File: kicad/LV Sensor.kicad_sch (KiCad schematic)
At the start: 4 parts, among them U1 MCP2518FD-xQBB, U2 74LVC1G3157, U3 MSPM0C1104SDSGR, U4 ADS8689RUM

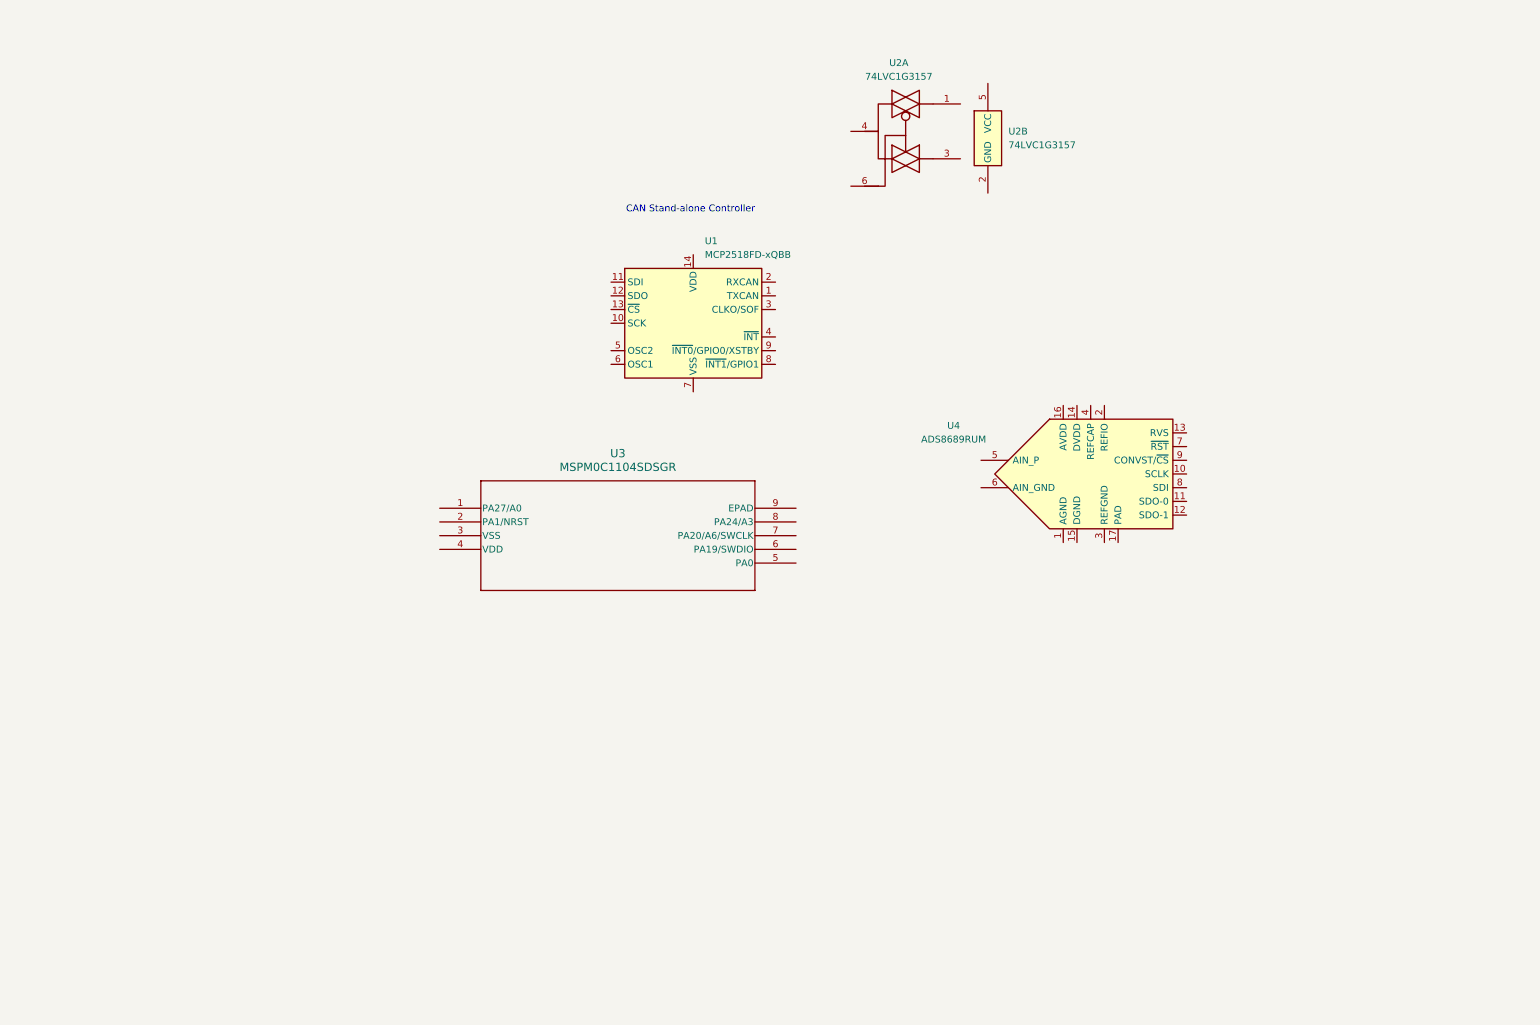
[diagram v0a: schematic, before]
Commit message: 08-25-25 Updated Board
Everything got deleted because a new copy was saved elsewhere.
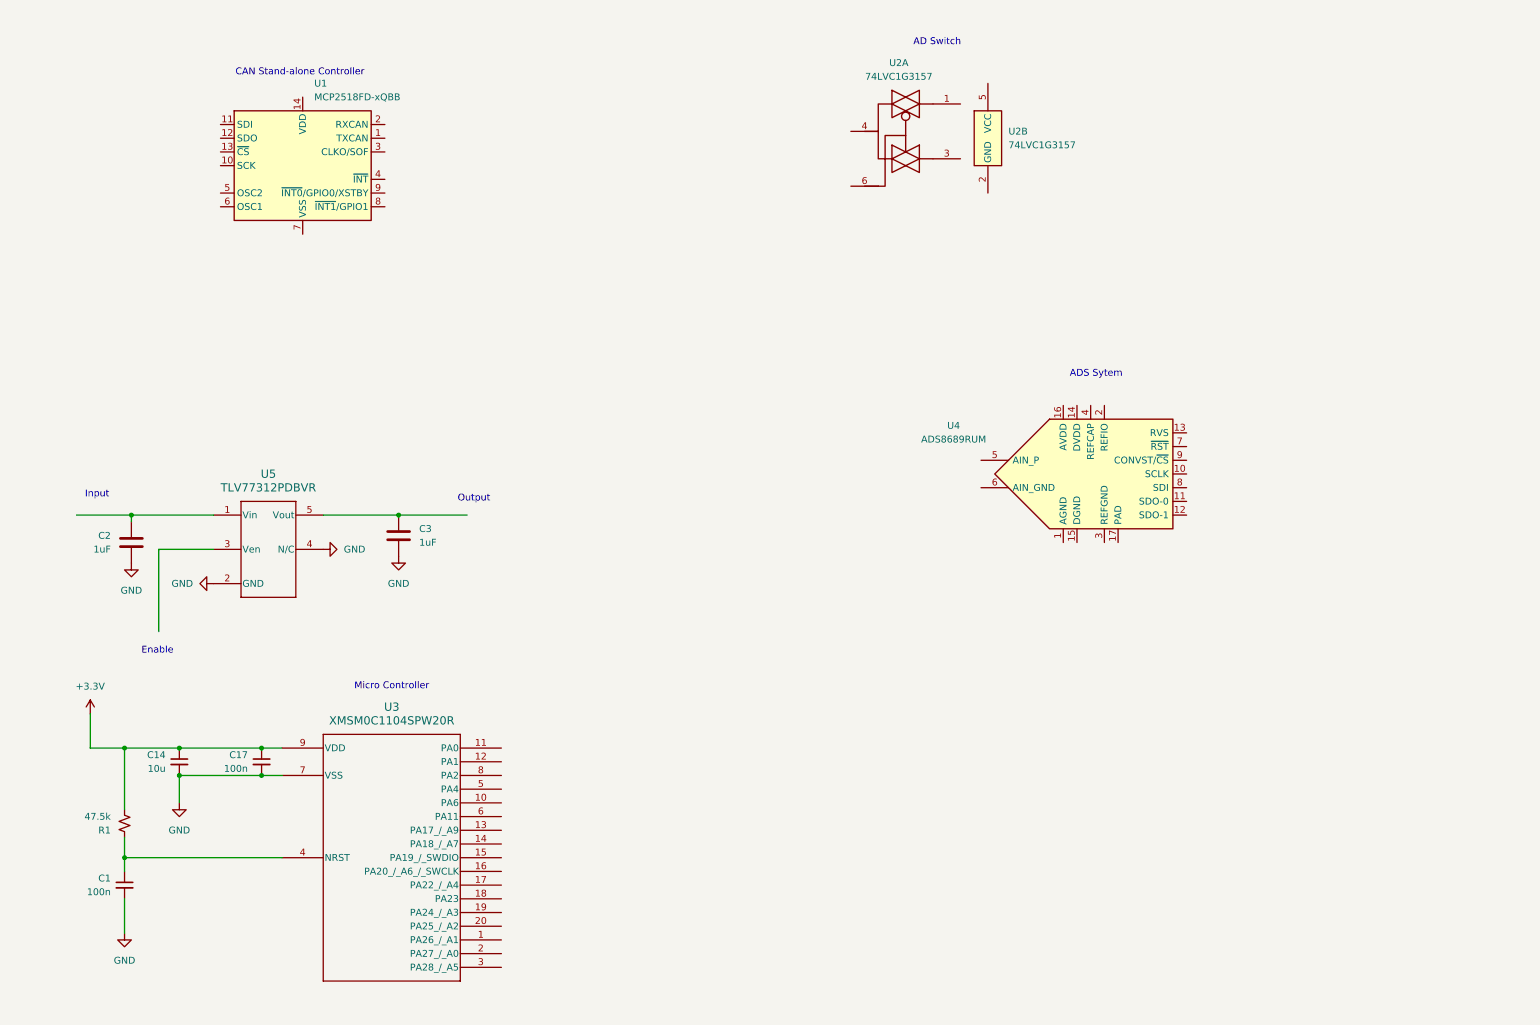
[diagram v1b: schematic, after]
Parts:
- removed U3: MSPM0C1104SDSGR, DSG0008A_TEX, symbol MSPM0C1104SDSGR:MSPM0C1104SDSGR
- added C1, C17: 100n, Capacitor_SMD:C_1206_3216Metric_Pad1.33x1.80mm_HandSolder, symbol Device:C_Small
- added C14: 10u, Capacitor_SMD:C_1206_3216Metric_Pad1.33x1.80mm_HandSolder, symbol Device:C_Small
- added C2, C3: 1uF, symbol Device:C
- added R1: 47.5k, Resistor_SMD:R_1206_3216Metric_Pad1.30x1.75mm_HandSolder, symbol Device:R_Small_US
- added U3: XMSM0C1104SPW20R, TSSOP20_PW_TEX, symbol MSPM0C1104-TSSOP:XMSM0C1104SPW20R
- added U5: TLV77312PDBVR, DBV0005A-IPC_A, symbol TLV77333PDBVR:TLV77312PDBVR
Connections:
- new net: C2.1, U5.1 (Vin)
- new net: C3.1, U5.5 (Vout)
- new net: C1.1, R1.1, U3.4 (NRST)
- new net +3.3V: C14.1, C17.1, R1.2, U3.9 (VDD)
- new net GND: C1.2, C14.2, C17.2, C2.2, C3.2, U3.7 (VSS), U5.2 (GND), U5.4 (N/C)
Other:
- note added: "AD Switch"
- note added: "ADS Sytem"
- note added: "Enable"
- note added: "Input"
- note added: "Micro Controller"
- note added: "Output"
- moved on the sheet: U1

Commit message: 06-26-25 Added OP Amplifier to schematic
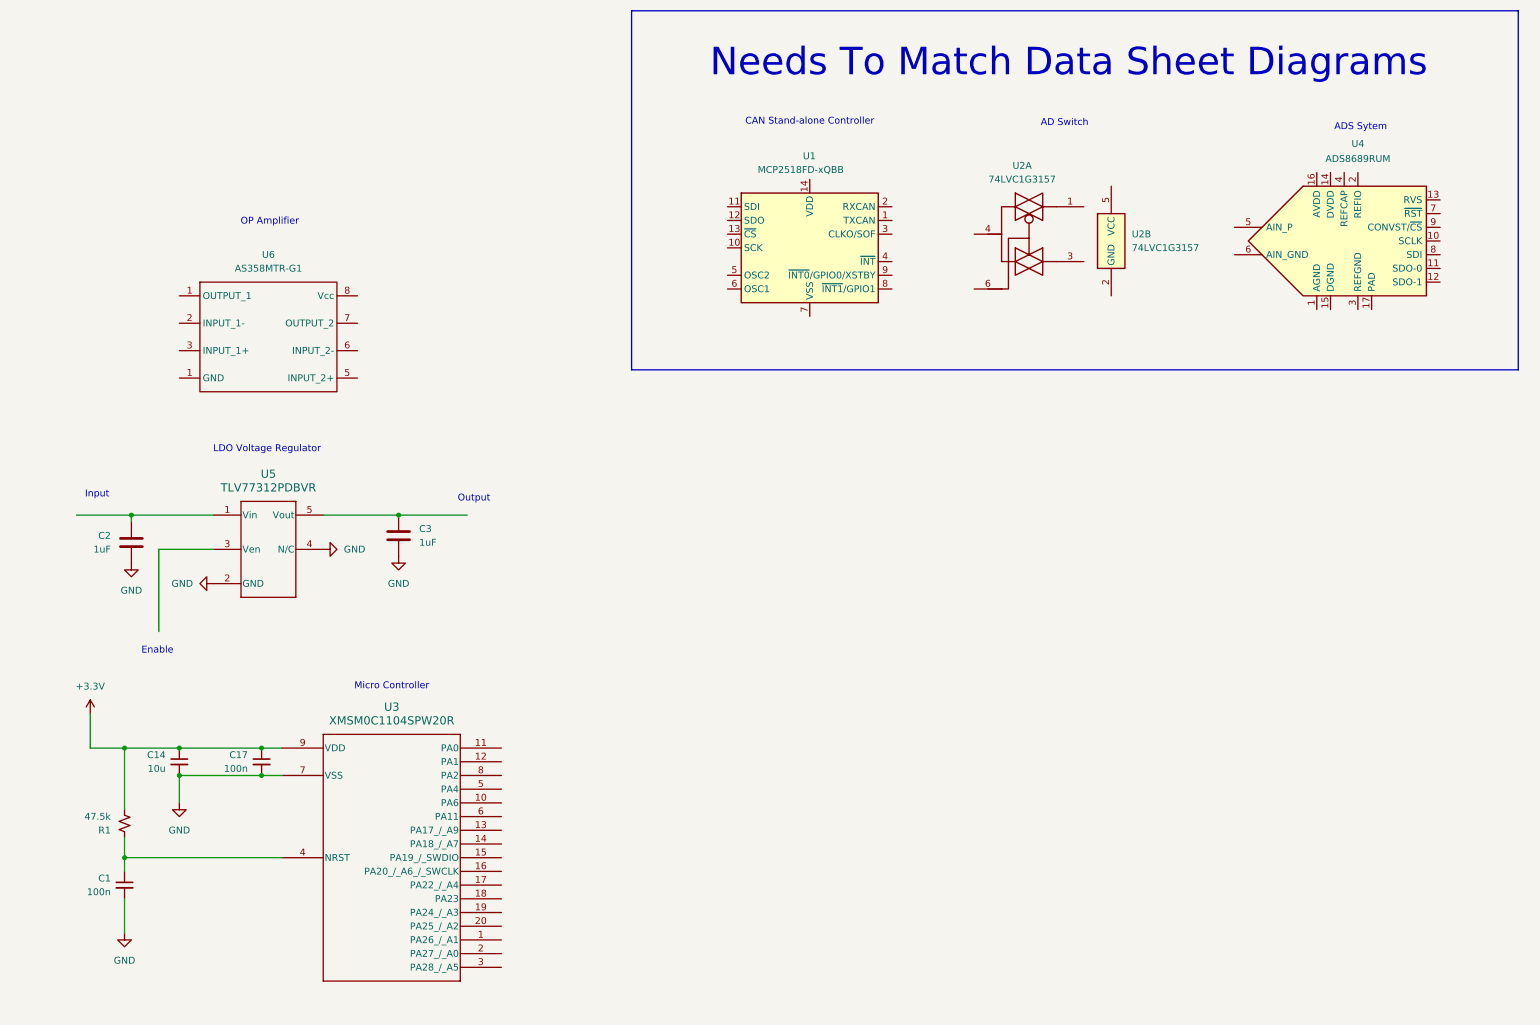
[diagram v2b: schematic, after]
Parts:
- added U6: AS358MTR-G1, symbol LV-Sensor-Lib:AS358MTR-G1
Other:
- note added: "LDO Voltage Regulator"
- note added: "Needs To Match Data Sheet Diagrams"
- note added: "OP Amplifier"
- company: (none) -> UTA FSAE
- title: (none) -> Low Voltage Sensor
- moved on the sheet: U1, U2A, U2B, U4
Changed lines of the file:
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@@
 	(generator_version "9.0")
 	(paper "A4")
+	(title_block
+		(title "Low Voltage Sensor")
+		(date "08-22-25")
+		(rev "0.1")
+		(company "UTA FSAE")
+	)
+	(rectangle
+		(start 120.65 11.938)
+		(end 284.988 78.486)
+		(stroke
+			(width 0)
+			(type default)
+		)
+		(fill
+			(type none)
+		)
+	)
 	(text "AD Switch"
 		(exclude_from_sim no)
-		(at 177.292 17.78 0)
+		(at 200.914 32.766 0)
+		(effects
+			(font
+				(size 1.27 1.27)
+			)
+		)
+	)
+	(text "LDO Voltage Regulator"
+		(exclude_from_sim no)
+		(at 53.086 93.218 0)
 		(effects
 			(font
@@
 	(text "CAN Stand-alone Controller"
 		(exclude_from_sim no)
-		(at 59.182 23.368 0)
+		(at 153.67 32.512 0)
 		(effects
 			(font
@@
 	(text "ADS Sytem"
 		(exclude_from_sim no)
-		(at 206.756 79.248 0)
+		(at 255.778 33.528 0)
 		(effects
 			(font
@@
 		(exclude_from_sim no)
 		(at 91.44 102.362 0)
+		(effects
+			(font
+				(size 1.27 1.27)
+			)
+		)
+	)
+	(text "Needs To Match Data Sheet Diagrams"
+		(exclude_from_sim no)
+		(at 201.676 21.59 0)
+		(effects
+			(font
+				(size 5.08 5.08)
+			)
+		)
+	)
+	(text "OP Amplifier"
+		(exclude_from_sim no)
+		(at 53.594 51.054 0)
 		(effects
 			(font
@@
 	(symbol
 		(lib_id "Interface_CAN_LIN:MCP2518FD-xQBB")
-		(at 59.69 40.64 0)
+		(at 153.67 55.88 0)
 		(unit 1)
 		(exclude_from_sim no)
@@
 		(on_board yes)
 		(dnp no)
-		(fields_autoplaced yes)
 		(property "Reference" "U1"
-			(at 61.8333 25.4 0)
+			(at 152.4 38.862 0)
 			(effects
 				(font
@@
 		)
 		(property "Value" "MCP2518FD-xQBB"
-			(at 61.8333 27.94 0)
+			(at 144.018 41.402 0)
 			(effects
 				(font
@@
 		)
 		(property "Footprint" "Package_DFN_QFN:DFN-14-1EP_3x4.5mm_P0.65mm_EP1.65x4.25mm"
-			(at 60.96 54.61 0)
+			(at 154.94 69.85 0)
 			(effects
 				(font
@@
 		)
 		(property "Datasheet" "https://ww1.microchip.com/downloads/aemDocuments/documents/OTH/ProductDocuments/DataSheets/External-CAN-FD-Controller-with-SPI-Interface-DS20006027B.pdf"
-			(at 60.96 57.15 0)
+			(at 154.94 72.39 0)
 			(effects
 				(font
@@
 		)
 		(property "Description" "CAN FD Controller with SPI Interface, up to 8 Mbps, Vdd 2.7..5.5V,  functional safety ready, VDFN-14"
-			(at 59.69 40.64 0)
+			(at 153.67 55.88 0)
 			(effects
 				(font
@@
 	)
 	(symbol
-		(lib_id "Analog_ADC:ADS8689RUM")
-		(at 203.2 97.79 0)
+		(lib_id "LV-Sensor-Lib:AS358MTR-G1")
+		(at 53.34 72.39 0)
 		(unit 1)
 		(exclude_from_sim no)
@@
 		(on_board yes)
 		(dnp no)
-		(fields_autoplaced yes)
+		(property "Reference" "U6"
+			(at 53.34 57.15 0)
+			(effects
+				(font
+					(size 1.27 1.27)
+				)
+			)
+		)
+		(property "Value" "AS358MTR-G1"
+			(at 53.34 59.69 0)
+			(effects
+				(font
+					(size 1.27 1.27)
+				)
+			)
+		)
+		(property "Footprint" ""
+			(at 53.34 77.47 0)
+			(effects
+				(font
+					(size 1.27 1.27)
+				)
+				(hide yes)
+			)
+		)
+		(property "Datasheet" "https://www.mouser.com/datasheet/2/115/DIOD_S_A0005046231_1-2542568.pdf"
+			(at 52.832 53.34 0)
+			(effects
+				(font
+					(size 1.27 1.27)
+					(color 194 194 194 1)
+				)
+				(hide yes)
+			)
+		)
+		(property "Description" ""
+			(at 53.34 77.47 0)
+			(effects
+				(font
+					(size 1.27 1.27)
+				)
+				(hide yes)
+			)
+		)
+		(property "mouser" "https://www.mouser.com/ProductDetail/Diodes-Incorporated/AS358MTR-G1?qs=FKu9oBikfSlRUA%2BzgDv25w%3D%3D"
+			(at 53.34 51.054 0)
+			(effects
+				(font
+					(size 1.27 1.27)
+				)
+				(hide yes)
+			)
+		)
+		(property "specs" "2 mV offset, 3 V, +/- 1.5 V, Max  36 V, +/- 18 V , 60 dB, -40C, +85C"
+			(at 52.832 48.26 0)
+			(effects
+				(font
+					(size 1.27 1.27)
+				)
+				(hide yes)
+			)
+		)
+		(property "unit x10" "0.089"
+			(at 58.42 77.47 0)
+			(effects
+				(font
+					(size 1.27 1.27)
+				)
+				(hide yes)
+			)
+		)
+		(pin "8"
+		)
+		(pin "1"
+		)
+		(pin "5"
+		)
+		(pin "2"
+		)
+		(pin "3"
+		)
+		(pin "1"
+		)
+		(pin "7"
+		)
+		(pin "6"
+		)
+		(instances
+			(project ""
+				(path "/1afce36f-b357-4e2a-9166-a84df6dcc281"
+					(reference "U6")
+					(unit 1)
+				)
+			)
+		)
+	)
+	(symbol
+		(lib_id "Analog_ADC:ADS8689RUM")
+		(at 250.19 54.61 0)
+		(unit 1)
+		(exclude_from_sim no)
+		(in_bom yes)
+		(on_board yes)
+		(dnp no)
 		(property "Reference" "U4"
-			(at 180.34 88.8298 0)
+			(at 255.27 36.576 0)
 			(effects
 				(font
@@
 		)
 		(property "Value" "ADS8689RUM"
-			(at 180.34 91.3698 0)
+			(at 255.27 39.37 0)
 			(effects
 				(font
@@
 		)
 		(property "Footprint" "Package_DFN_QFN:QFN-16-1EP_4x4mm_P0.65mm_EP2.7x2.7mm"
-			(at 203.2 120.65 0)
+			(at 250.19 77.47 0)
 			(effects
 				(font
@@
 		)
 		(property "Datasheet" "http://www.ti.com/lit/ds/symlink/ads8681.pdf"
-			(at 204.47 91.44 0)
+			(at 251.46 48.26 0)
 			(effects
 				(font
@@
 		)
 		(property "Description" "16-Bit, High-Speed, Single-Supply, SAR ADC Data Acquisition System with Programmable, Bipolar Input Ranges, 100KSPS, QFN-16"
-			(at 203.2 97.79 0)
+			(at 250.19 54.61 0)
 			(effects
 				(font
@@
 	(symbol
 		(lib_id "74xGxx:74LVC1G3157")
-		(at 186.69 35.56 0)
+		(at 209.55 54.61 0)
 		(unit 2)
 		(exclude_from_sim no)
@@
 		(fields_autoplaced yes)
 		(property "Reference" "U2"
-			(at 190.5 34.2899 0)
+			(at 213.36 53.3399 0)
 			(effects
 				(font
@@
 		)
 		(property "Value" "74LVC1G3157"
-			(at 190.5 36.8299 0)
+			(at 213.36 55.8799 0)
 			(effects
 				(font
@@
 		)
 		(property "Footprint" ""
-			(at 186.69 35.56 0)
+			(at 209.55 54.61 0)
 			(effects
 				(font
@@
 		)
 		(property "Datasheet" "http://www.ti.com/lit/sg/scyt129e/scyt129e.pdf"
-			(at 186.69 35.56 0)
+			(at 209.55 54.61 0)
 			(effects
 				(font
@@
 		)
 		(property "Description" "SPDT Analog Switch, Low-Voltage CMOS"
-			(at 186.69 35.56 0)
+			(at 209.55 54.61 0)
 			(effects
 				(font
@@
 	(symbol
 		(lib_id "74xGxx:74LVC1G3157")
-		(at 171.45 34.29 0)
+		(at 194.31 53.34 0)
 		(unit 1)
 		(exclude_from_sim no)
@@
 		(fields_autoplaced yes)
 		(property "Reference" "U2"
-			(at 170.18 21.59 0)
+			(at 193.04 40.64 0)
 			(effects
 				(font
@@
 		)
 		(property "Value" "74LVC1G3157"
-			(at 170.18 24.13 0)
+			(at 193.04 43.18 0)
 			(effects
 				(font
@@
 		)
 		(property "Footprint" ""
-			(at 171.45 34.29 0)
+			(at 194.31 53.34 0)
 			(effects
 				(font
@@
 		)
 		(property "Datasheet" "http://www.ti.com/lit/sg/scyt129e/scyt129e.pdf"
-			(at 171.45 34.29 0)
+			(at 194.31 53.34 0)
 			(effects
 				(font
@@
 		)
 		(property "Description" "SPDT Analog Switch, Low-Voltage CMOS"
-			(at 171.45 34.29 0)
-			(effects
-				(font
+			(at 194.31 53.34 0)
+			(effects
+				(font

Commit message: something
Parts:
- removed C1, C17: 100n, Capacitor_SMD:C_1206_3216Metric_Pad1.33x1.80mm_HandSolder, symbol Device:C_Small
- removed C14: 10u, Capacitor_SMD:C_1206_3216Metric_Pad1.33x1.80mm_HandSolder, symbol Device:C_Small
- removed C2, C3: 1uF, symbol Device:C
- removed R1: 47.5k, Resistor_SMD:R_1206_3216Metric_Pad1.30x1.75mm_HandSolder, symbol Device:R_Small_US
- removed U1: MCP2518FD-xQBB, Package_DFN_QFN:DFN-14-1EP_3x4.5mm_P0.65mm_EP1.65x4.25mm, symbol Interface_CAN_LIN:MCP2518FD-xQBB
- removed U2: 74LVC1G3157, symbol 74xGxx:74LVC1G3157
- removed U3: XMSM0C1104SPW20R, TSSOP20_PW_TEX, symbol MSPM0C1104-TSSOP:XMSM0C1104SPW20R
- removed U4: ADS8689RUM, Package_DFN_QFN:QFN-16-1EP_4x4mm_P0.65mm_EP2.7x2.7mm, symbol Analog_ADC:ADS8689RUM
- removed U5: TLV77312PDBVR, DBV0005A-IPC_A, symbol TLV77333PDBVR:TLV77312PDBVR
- removed U6: AS358MTR-G1, symbol LV-Sensor-Lib:AS358MTR-G1
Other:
- added sheet AD Switch (LV Sensor-AD Switch.kicad_sch)
- added sheet ADC System (LV Sensor-ADC System.kicad_sch)
- added sheet CAN Stand-alone Controller (LV Sensor-CAN Stand-alone Controller.kicad_sch)
- added sheet LDO Voltage Regulator (LV Sesnsor-LDO Voltage Regulator.kicad_sch)
- added sheet Micro Controller (LV Sensor-Micro Controller.kicad_sch)
- added sheet OP Amplifier (LV Sensor-OP Amplifier.kicad_sch)
- note added: "Needs A Footprint"
- note removed: "AD Switch"
- note removed: "ADS Sytem"
- note removed: "CAN Stand-alone Controller"
- note removed: "Enable"
- note removed: "Input"
- note removed: "LDO Voltage Regulator"
- note removed: "Micro Controller"
- note removed: "Needs To Match Data Sheet Diagrams"
- note removed: "OP Amplifier"
- note removed: "Output"

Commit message: sdfafsdfsfdaf
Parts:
- added C1, C17: 100n, Capacitor_SMD:C_1206_3216Metric_Pad1.33x1.80mm_HandSolder, symbol Device:C_Small
- added C14: 10u, Capacitor_SMD:C_1206_3216Metric_Pad1.33x1.80mm_HandSolder, symbol Device:C_Small
- added C2, C3: 1uF, symbol Device:C
- added R1: 47.5k, Resistor_SMD:R_1206_3216Metric_Pad1.30x1.75mm_HandSolder, symbol Device:R_Small_US
- added U1: MCP2518FD-xJHA, LV Sensor:MCP2518FDT, symbol LV-Sensor-Lib:MCP2517FD-xJHA
- added U2: 74LVC1G3157GW_125, LV Sensor:74LVC1G3157GW_SOT363-2, symbol 74LVC1G3157GW_125:74LVC1G3157GW_125
- added U3: XMSM0C1104SPW20R, TSSOP20_PW_TEX, symbol MSPM0C1104-TSSOP:XMSM0C1104SPW20R
- added U4: ADS8689TSSOP, Package_DFN_QFN:QFN-16-1EP_4x4mm_P0.65mm_EP2.7x2.7mm, symbol LV-Sensor-Lib:ADS8689TSSOP
- added U5: TLV77312PDBVR, DBV0005A-IPC_A, symbol TLV77333PDBVR:TLV77312PDBVR
- added U6: AS358MTR-G1, symbol LV-Sensor-Lib:AS358MTR-G1
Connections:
- new net: C1.1, R1.1, U3.4 (NRST)
- new net +3.3V: C14.1, C17.1, R1.2, U1.14 (VDD), U2.5 (VCC), U3.9 (VDD), U6.8 (Vcc)
- new net ENABLE: U5.3 (Ven)
- new net GND: C1.2, C14.2, C17.2, C2.2, C3.2, U1.5 (OSC2), U1.6 (OSC1), U1.7 (VSS), U2.2 (GND), U3.7 (VSS), U5.2 (GND), U5.4 (N/C), U6.1 (GND)
- new net Input: C2.1, U5.1 (Vin)
- new net OUTPUT: C3.1, U5.5 (Vout)
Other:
- removed sheet AD Switch
- removed sheet ADC System
- removed sheet CAN Stand-alone Controller
- removed sheet LDO Voltage Regulator
- removed sheet Micro Controller
- removed sheet OP Amplifier
- note added: "AD Switch"
- note added: "ADC System"
- note added: "CAN Oscillator"
- note added: "CAN Stand-alone Controller"
- note added: "LDO Voltage Regulator"
- note added: "Micro Controller"
- note added: "https://www.mouser.com/ProductDetail/Microchip-Technology/DSC1001DI5-004.0000?qs=8cKuZ6Ok2lZGbNNdo1eq1w%3D%3D"
- note removed: "Needs A Footprint"
